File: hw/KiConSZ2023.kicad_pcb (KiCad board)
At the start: 4 copper layers, 100 x 59.9 mm, 105 parts, among them J2 Conn_01x06, J3 USB_C_Receptacle_USB2.0, J4 Conn_02x03_Top_Bottom, J5 Conn_02x03_Top_Bottom, J6 BM20B(0.8)-10DS-0.4V, Q10 2N7002T, Q11 2N7002T, Q12 2N7002T, Q13 2N7002T, Q14 2N7002T, Q15 2N7002T, Q16 2N7002T, Q2 2N7002T, Q3 2N7002T, Q4 2N7002T, Q5 2N7002T, Q6 2N7002T, Q7 2N7002T, Q8 2N7002T, Q9 2N7002T, SW2 SKRPACE010, SW3 SKRPACE010, SW4 SW_SPDT, U2 N32L406RBL7, U3 PUSB3FR4, U4 AP3410K, U5 BL8536CB3xx

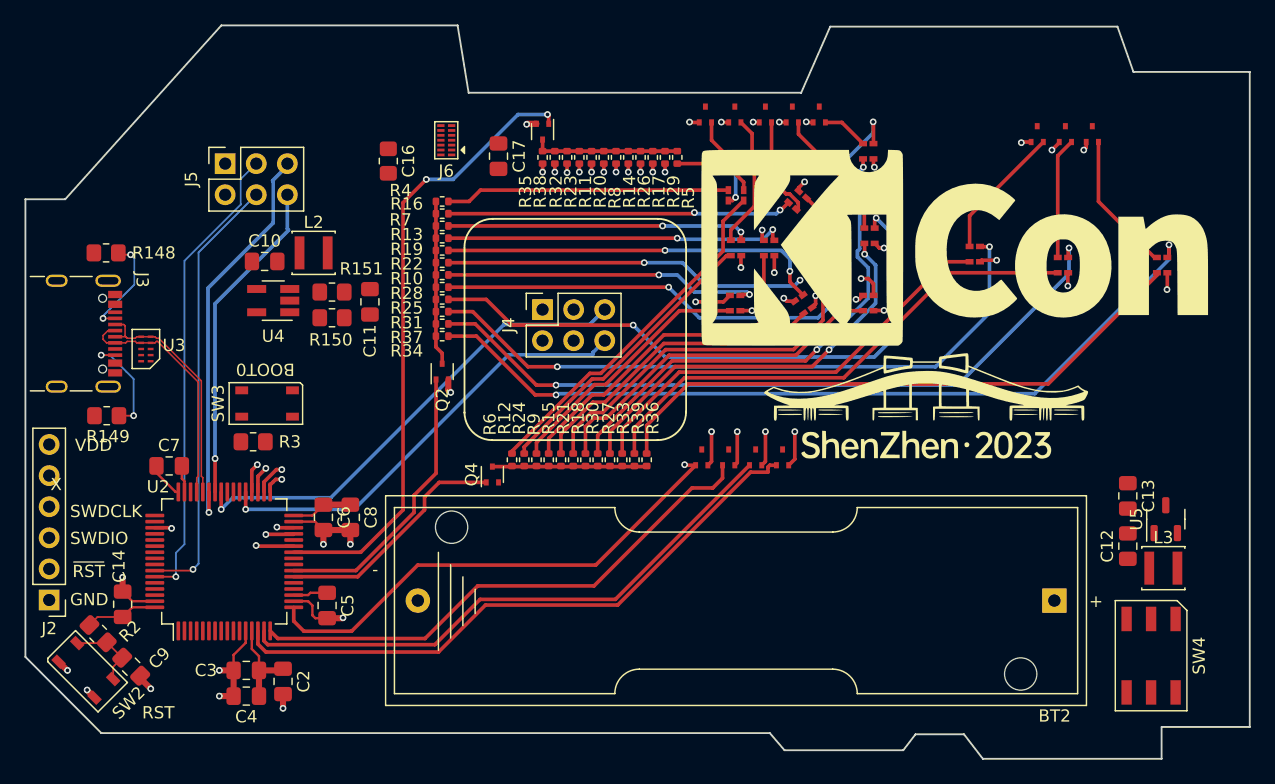
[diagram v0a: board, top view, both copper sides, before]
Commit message: routed VDDA
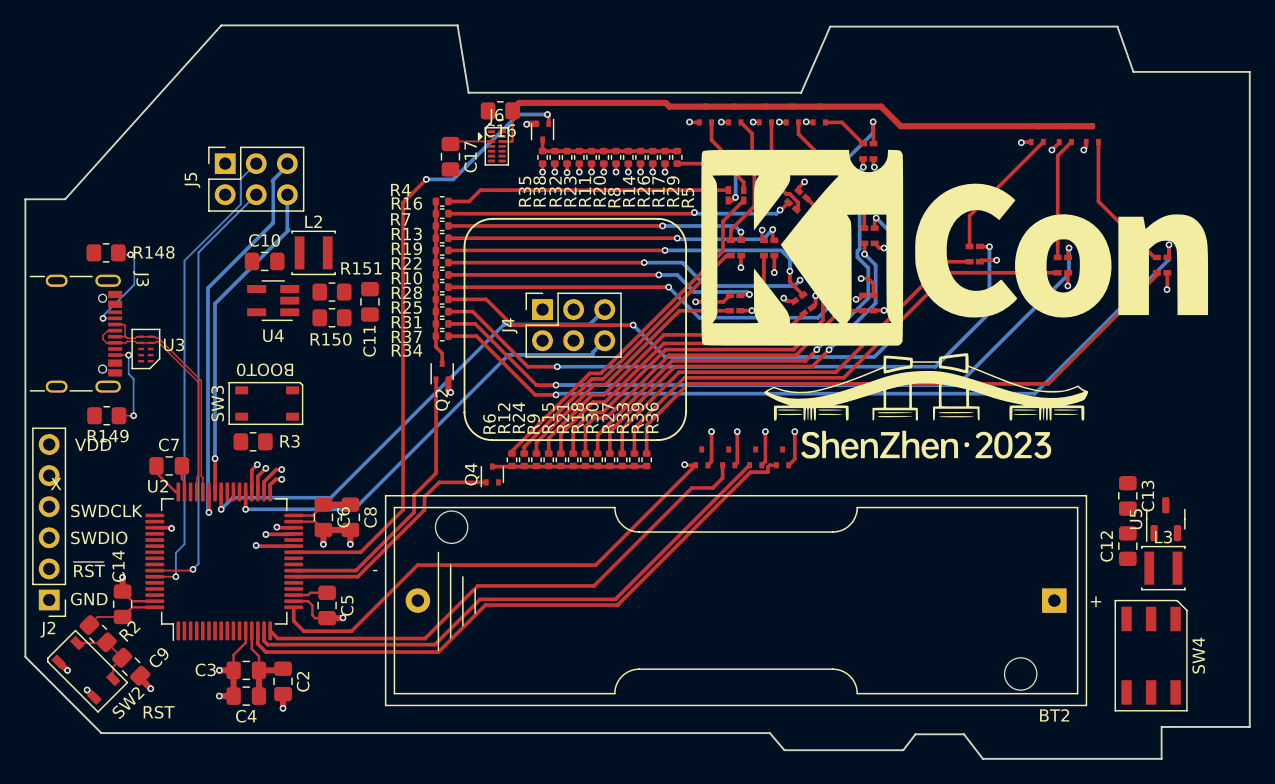
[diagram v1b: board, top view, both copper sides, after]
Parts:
- moved C16 10.0 mm to (89.0, 90.9), turned to 180 degrees
- moved J6 4.16 mm to (88.8, 93.8), turned to -90 degrees
- moved C17 3.92 mm to (85.0, 94.7)
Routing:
- net VDDA: track 24.1 -> 75.9 mm
- net /DISP_DISP: track 0.00 -> 3.43 mm
- net /USB/CC2: track 8.80 -> 7.43 mm
- added copper zone on In1.Cu, net GND

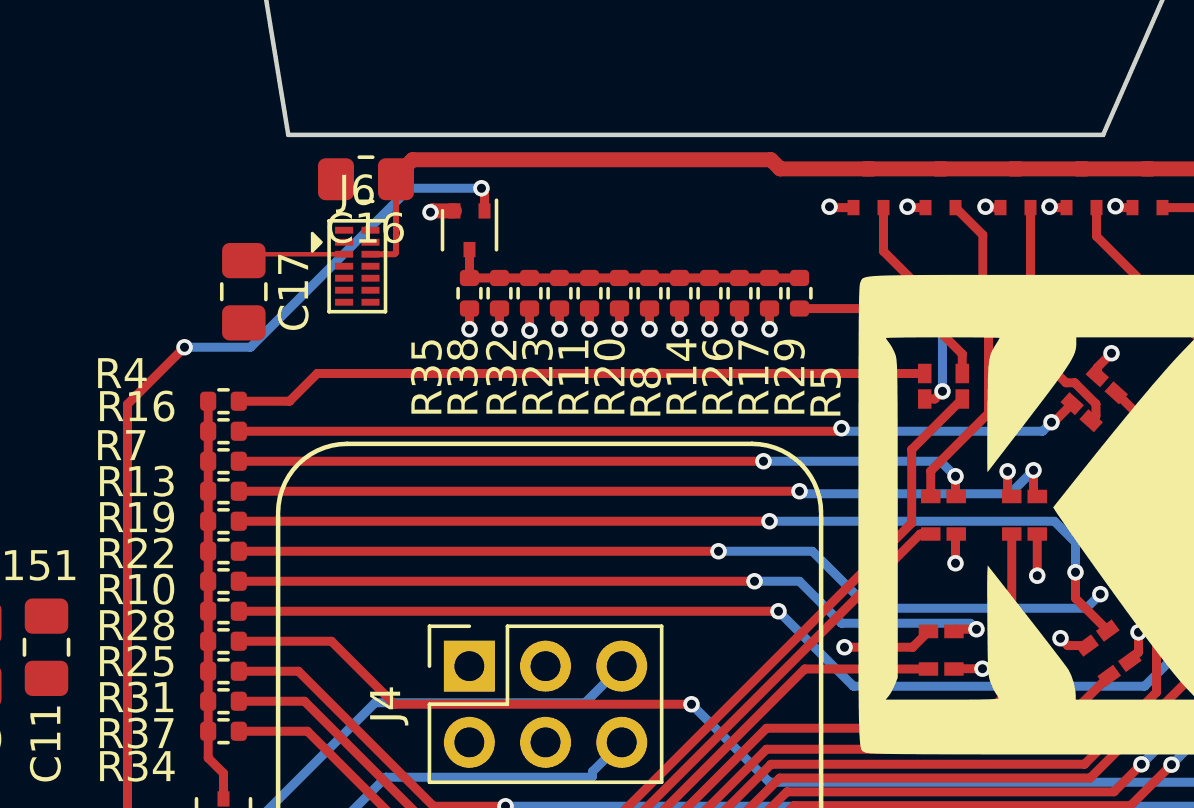
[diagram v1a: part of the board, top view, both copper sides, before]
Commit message: moved High Side Resistors
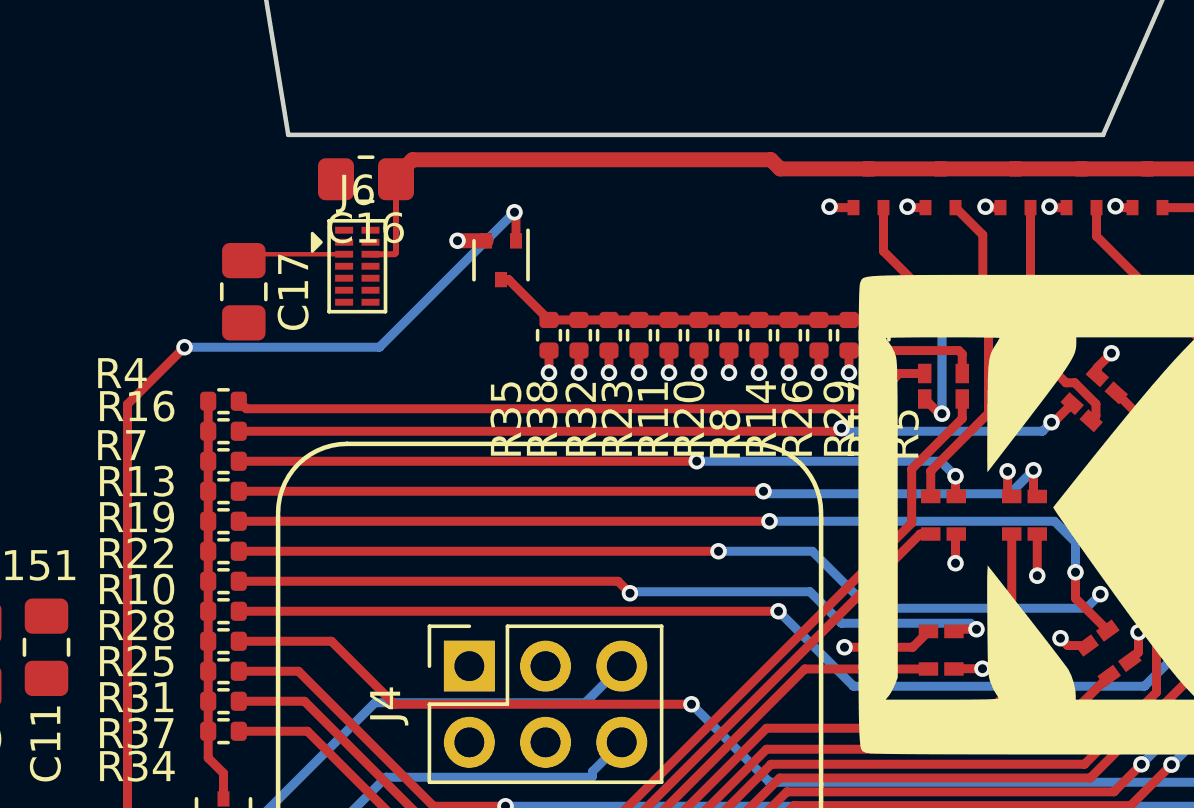
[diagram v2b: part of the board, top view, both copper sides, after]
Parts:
- moved R17 3.91 mm to (105.2, 96.1)
- moved R11 3.00 mm to (99.2, 96.1)
- moved R14 3.00 mm to (102.2, 96.1)
- moved R20 3.00 mm to (100.2, 96.1)
- moved R23 3.00 mm to (98.2, 96.1)
- moved R26 3.00 mm to (103.2, 96.1)
- moved R32 3.00 mm to (97.2, 96.1)
- moved R35 3.00 mm to (95.2, 96.1)
- moved R38 3.00 mm to (96.2, 96.1)
- moved R8 3.00 mm to (101.2, 96.1)
- moved R5 2.95 mm to (106.1, 96.1)
- moved R29 2.16 mm to (104.2, 96.1)
- moved Q3 1.45 mm to (93.5, 93.6)
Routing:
- net Net-(D9-GK): track 24.6 -> 20.9 mm
- net Net-(D6-GK): track 14.5 -> 10.7 mm
- net Net-(D2-GK): track 6.70 -> 3.52 mm
- net Net-(D5-GK): track 17.4 -> 14.2 mm
- net Net-(D7-GK): track 23.2 -> 20.1 mm
- net Net-(D3-GK): track 15.1 -> 12.0 mm
- net /HighSide_Row_2: track 60.7 -> 58.3 mm
- net Net-(D4-GK): track 19.6 -> 17.9 mm
- net Net-(D8-GK): track 41.3 -> 39.6 mm
- net /HighSide_Row_1: track 54.5 -> 53.0 mm
- net Net-(D12-GK): track 61.7 -> 60.3 mm
- net /SAO_SCL: track 66.8 -> 68.1 mm
- net Net-(D13-GK): track 50.0 -> 48.7 mm
- net Net-(D11-GK): track 43.0 -> 41.7 mm
- net Net-(D10-GK): track 18.8 -> 17.7 mm
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
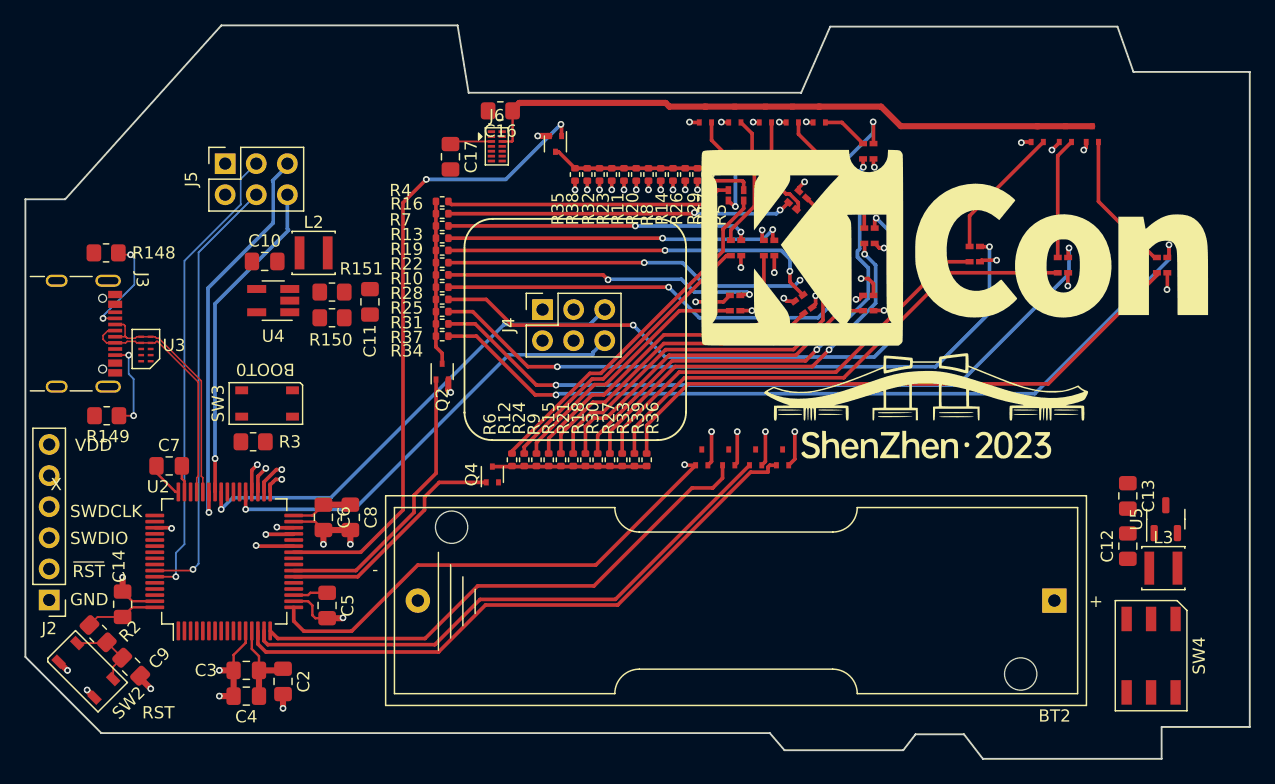
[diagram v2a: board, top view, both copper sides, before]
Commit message: re-arrange high side resistors
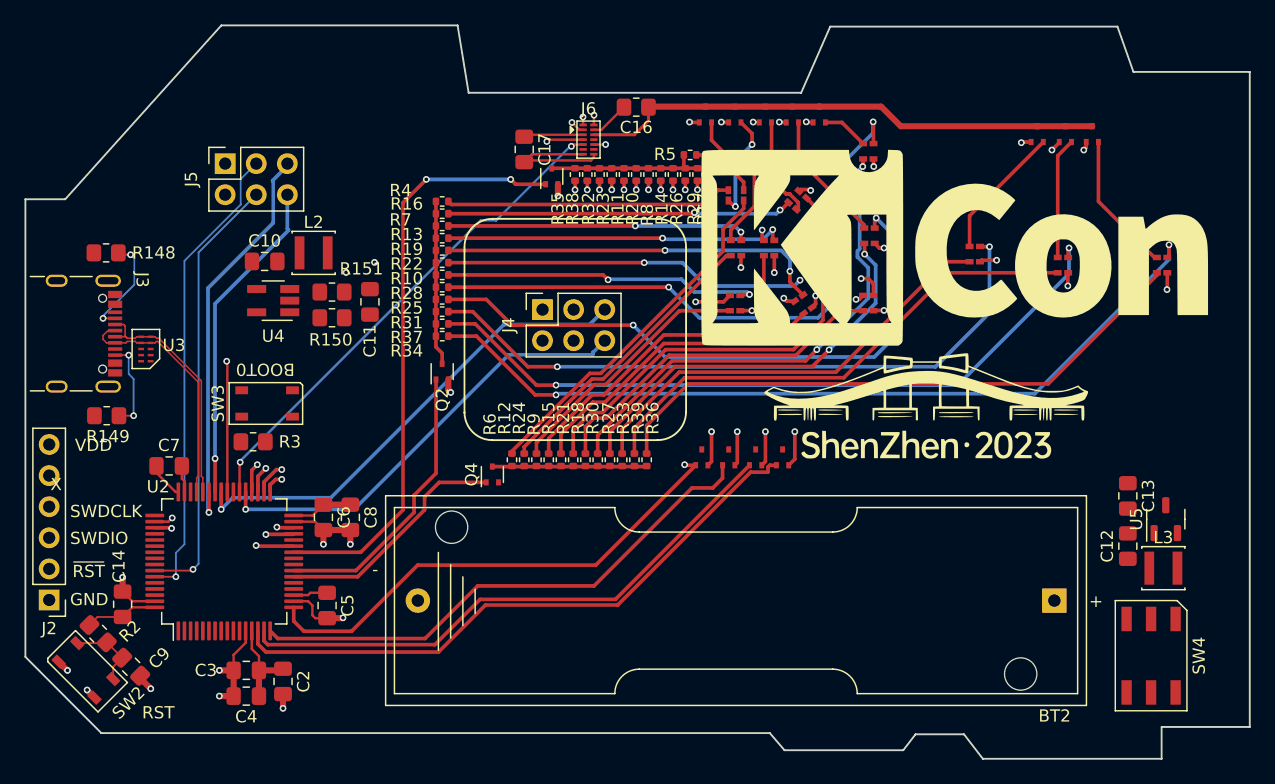
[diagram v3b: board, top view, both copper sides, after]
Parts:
- moved C16 11.1 mm to (100.2, 90.6)
- moved J6 7.51 mm to (96.2, 93.2)
- moved C17 6.05 mm to (91.0, 94.0)
- moved Q3 2.67 mm to (93.2, 96.2), turned to 90 degrees
- moved R5 2.23 mm to (104.5, 94.5), turned to 180 degrees
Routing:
- net /DISP_MOSI: track 0.00 -> 50.6 mm, vias 0 -> 2
- net /DISP_~{SS}: track 0.00 -> 48.5 mm, vias 0 -> 2
- net /DISP_SCK: track 0.00 -> 41.3 mm, vias 0 -> 2
- net GND: track 33.3 -> 50.3 mm, vias 12 -> 15
- net VDDA: track 75.9 -> 67.1 mm
- net /LowSide_G_Col_1: track 52.0 -> 48.1 mm
- net /HighSide_Row_2: track 58.3 -> 60.2 mm
- net Net-(D2-GK): track 3.52 -> 5.44 mm
- net Net-(D11-GK): track 41.7 -> 40.2 mm
- net /DISP_DISP: track 3.43 -> 4.88 mm
- net /SAO_SCL: track 68.1 -> 66.8 mm, vias 1 -> 2
- net Net-(D8-GK): track 39.6 -> 38.6 mm
- net /SAO_SDA: track 69.8 -> 69.1 mm, vias 1 -> 2
- net Net-(D13-GK): track 48.7 -> 48.1 mm
- net Net-(D12-GK): track 60.3 -> 59.7 mm

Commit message: change routing high side
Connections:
- net VDDA renamed VDD
- U2 pad 27: /HighSide_Row_10 -> /HighSide_Row_12
- U2 pad 30: /HighSide_Row_12 -> /HighSide_Row_10
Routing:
- net /HighSide_Row_12: track 88.8 -> 94.0 mm
- net /HighSide_Row_10: track 90.7 -> 87.7 mm
- net /HighSide_Row_11: track 89.5 -> 90.8 mm

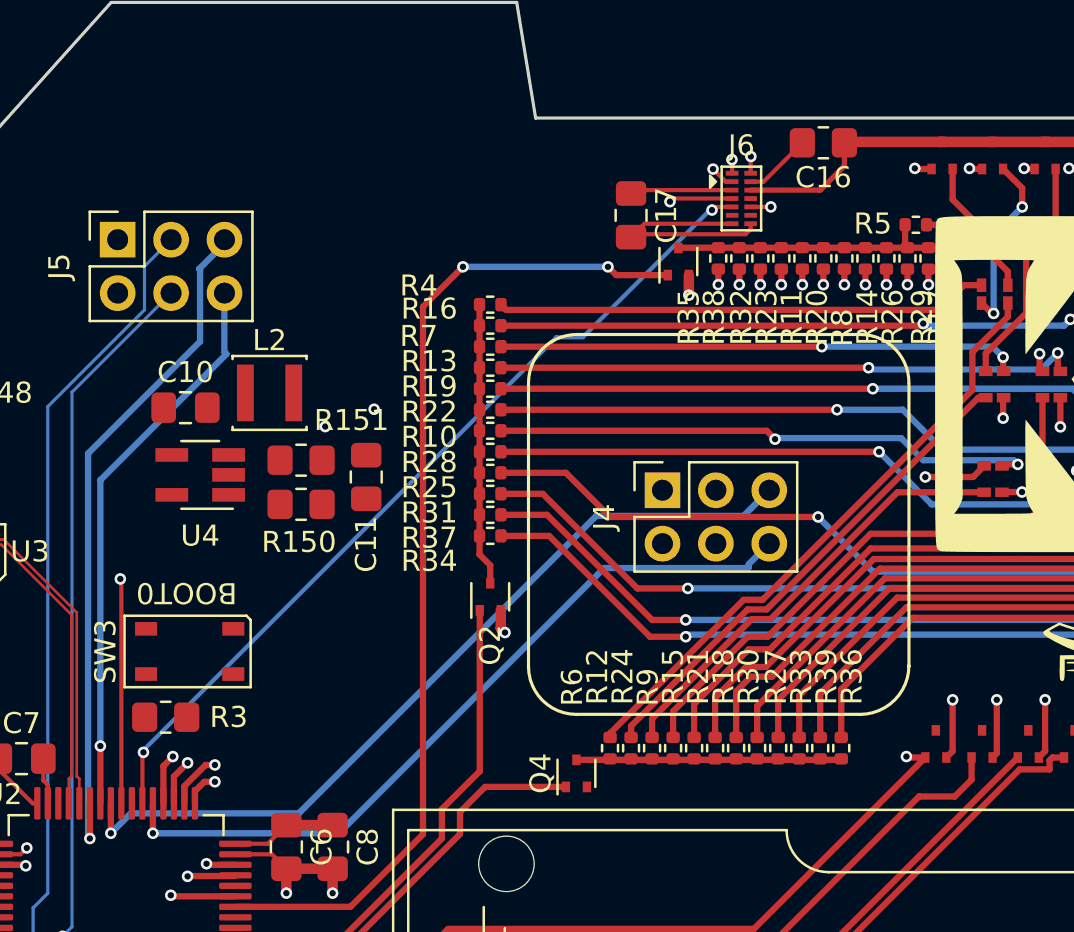
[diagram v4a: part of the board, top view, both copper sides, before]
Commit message: fix signal DISP_DISP
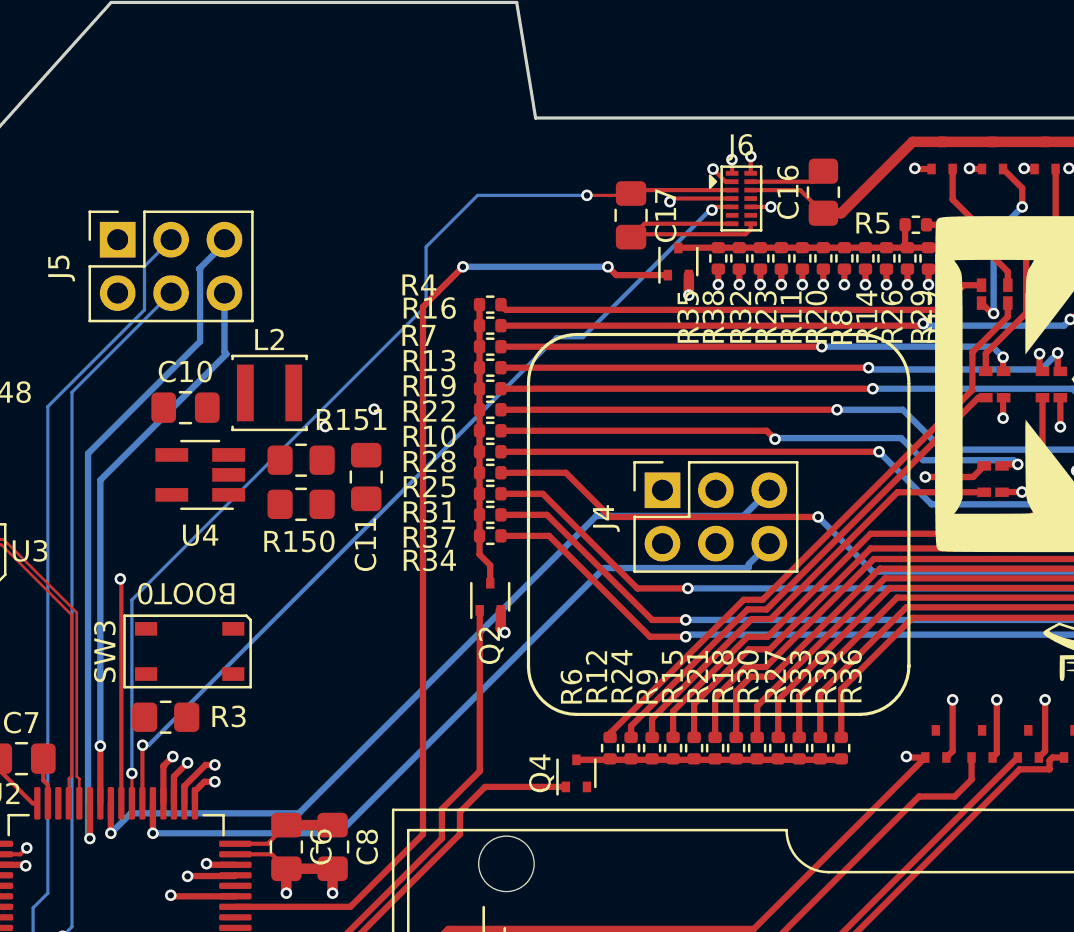
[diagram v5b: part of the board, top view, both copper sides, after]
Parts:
- moved C16 2.35 mm to (100.2, 93.0), turned to 90 degrees
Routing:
- net /DISP_DISP: track 4.88 -> 48.0 mm, vias 0 -> 2
